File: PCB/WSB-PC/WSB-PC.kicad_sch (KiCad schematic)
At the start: 35 parts, among them P1 GT-USB-8012A, SW1 SW_SPST_4_PIN, U1 74LV1T34, U2 ESP32-C6-MINI-1, U4 TPD2E2U06DRL, U5 NCP187

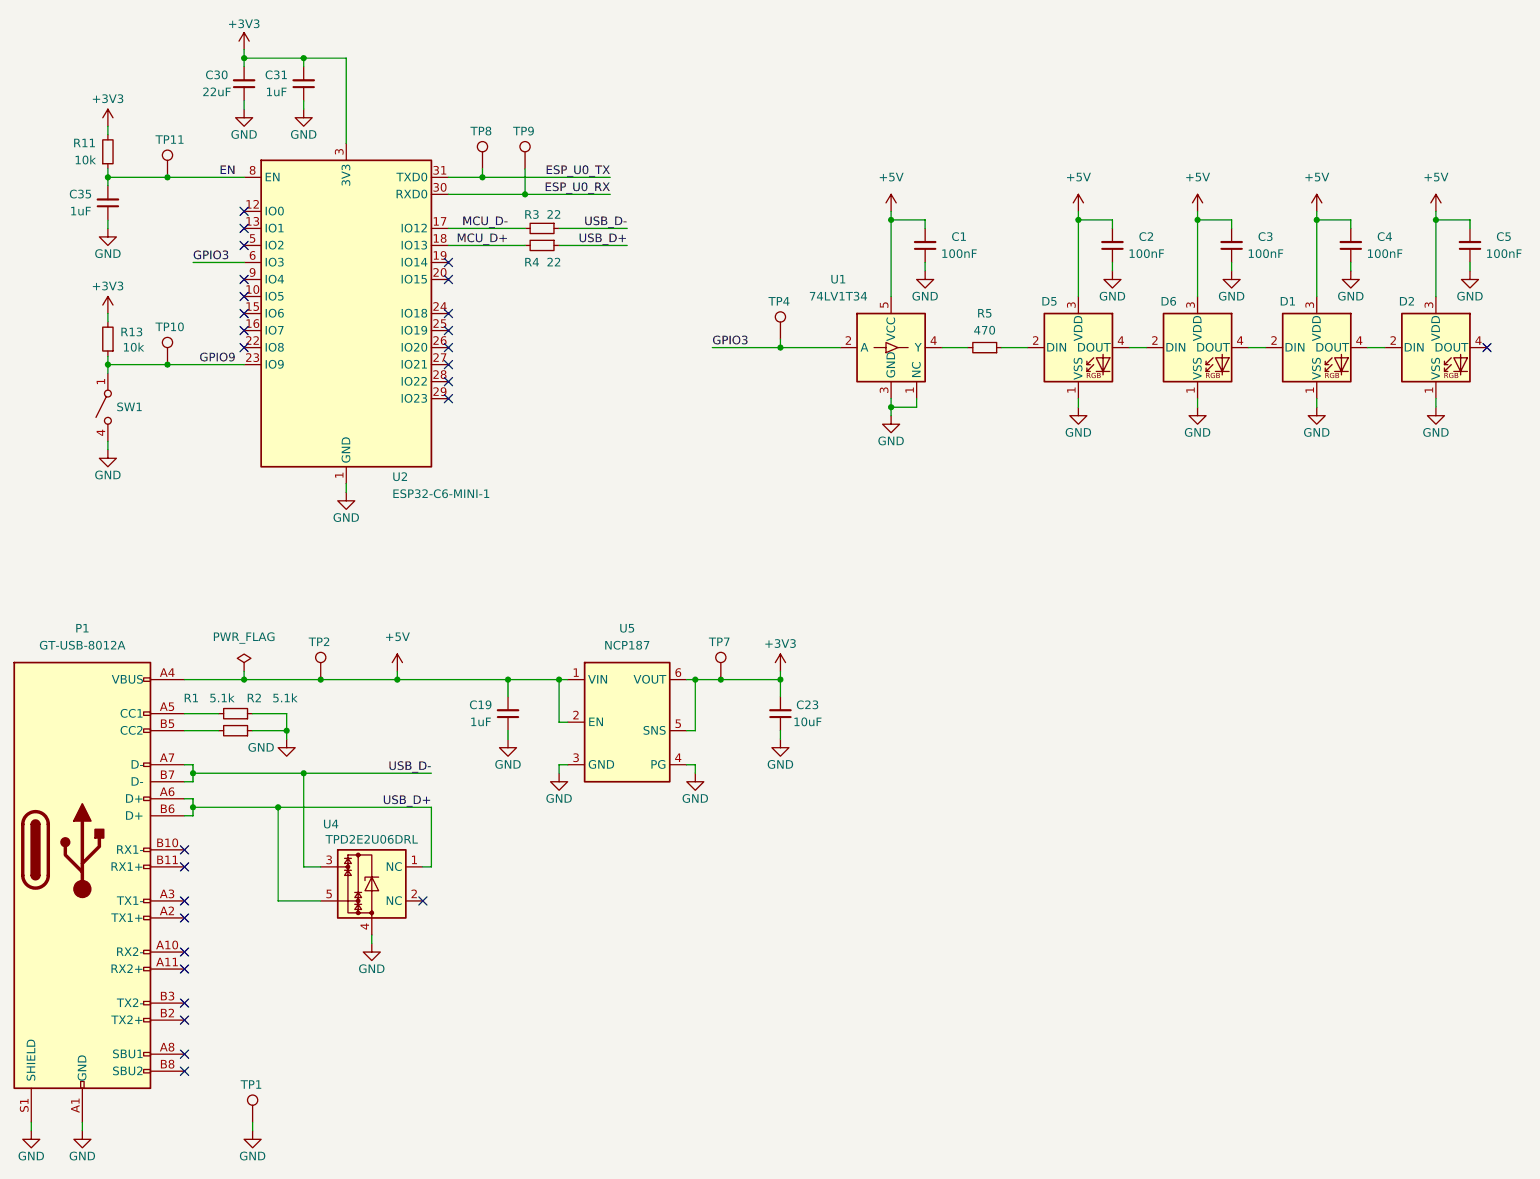
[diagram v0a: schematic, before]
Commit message: -Corrected test point numbering
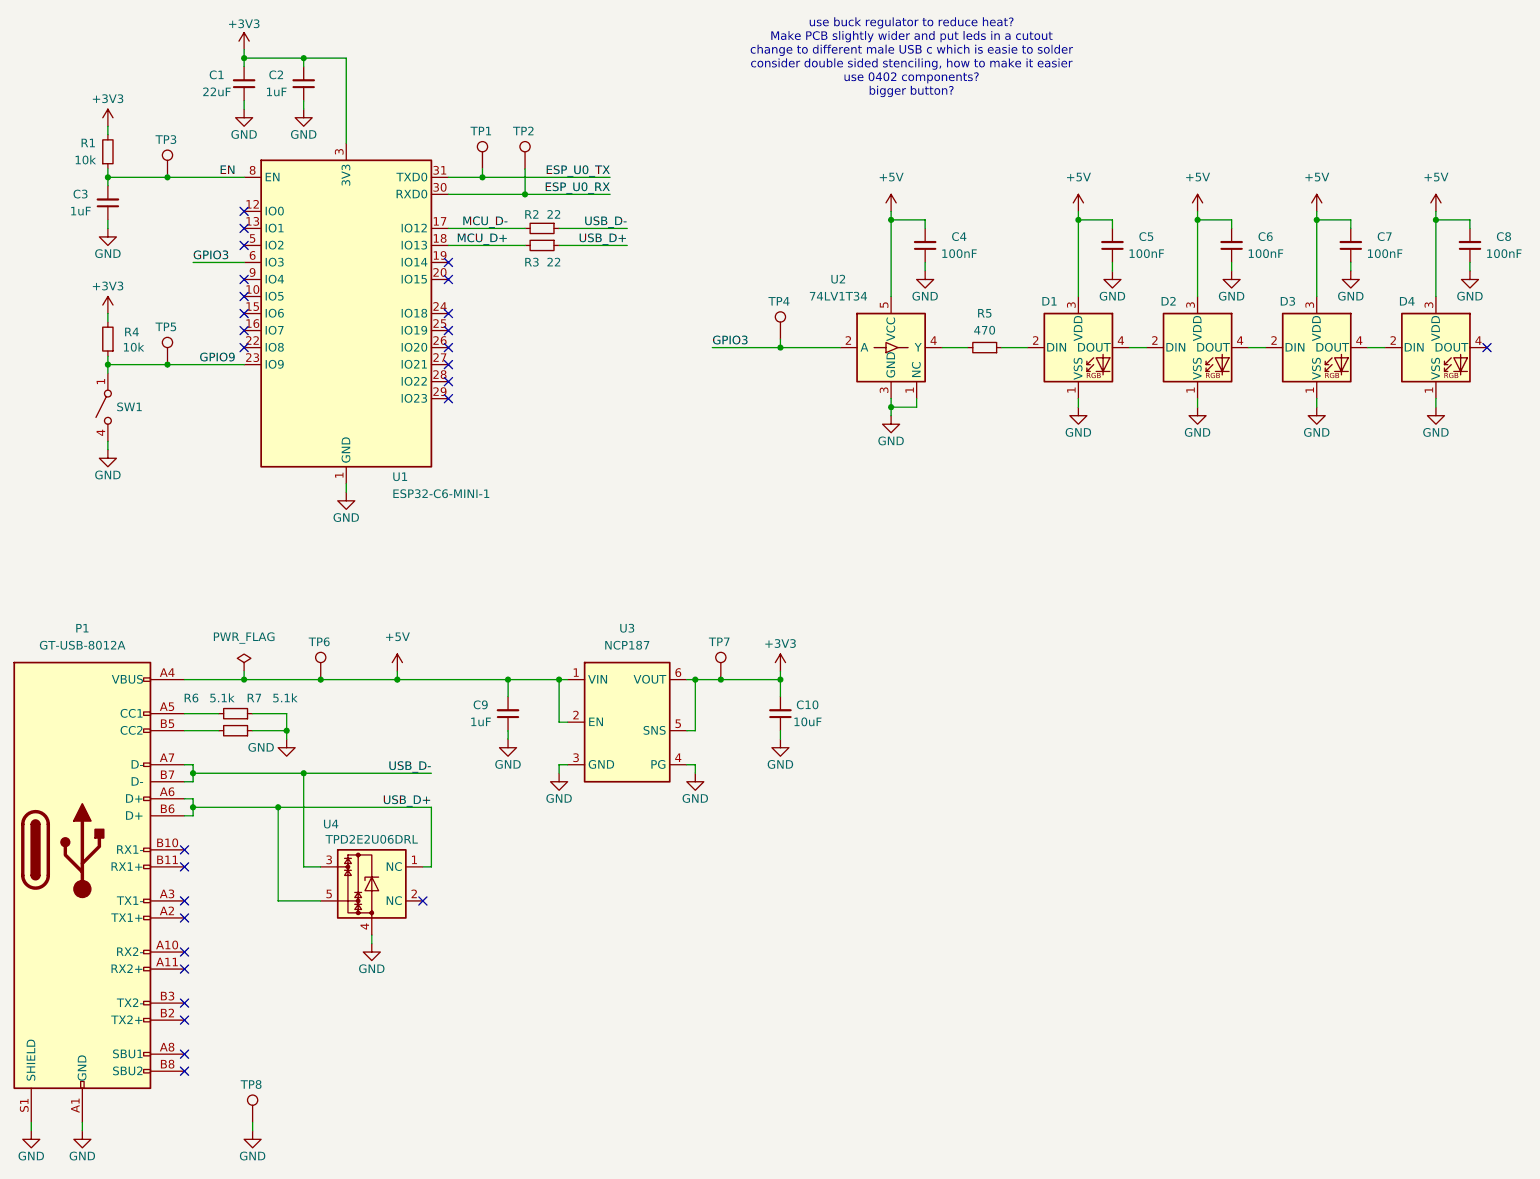
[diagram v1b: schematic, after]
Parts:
- renumbered C30 to C1, C23 to C10, C31 to C2, C35 to C3, C1 to C4, C2 to C5, C3 to C6, C4 to C7, C5 to C8, C19 to C9, D5 to D1, D6 to D2, D1 to D3, D2 to D4, R11 to R1, R3 to R2, R4 to R3, R13 to R4, R1 to R6, R2 to R7, TP8 to TP1, TP9 to TP2, TP11 to TP3, TP10 to TP5, TP2 to TP6, TP1 to TP8, U2 to U1, U1 to U2, U5 to U3
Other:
- note added: "use buck regulator to reduce heat? Make PCB slightly wider and put leds in a cutout change to different male USB c which is easie to solder consider double sided stenciling, how to make it easier use 0402 components? bigger button?"
